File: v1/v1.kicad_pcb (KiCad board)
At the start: 2 copper layers, 48.3 x 30.5 mm, 11 parts, among them J3 PWR, J4 RGB, U1 Lolin/WeMos_D1_mini, U2 LevelShifter

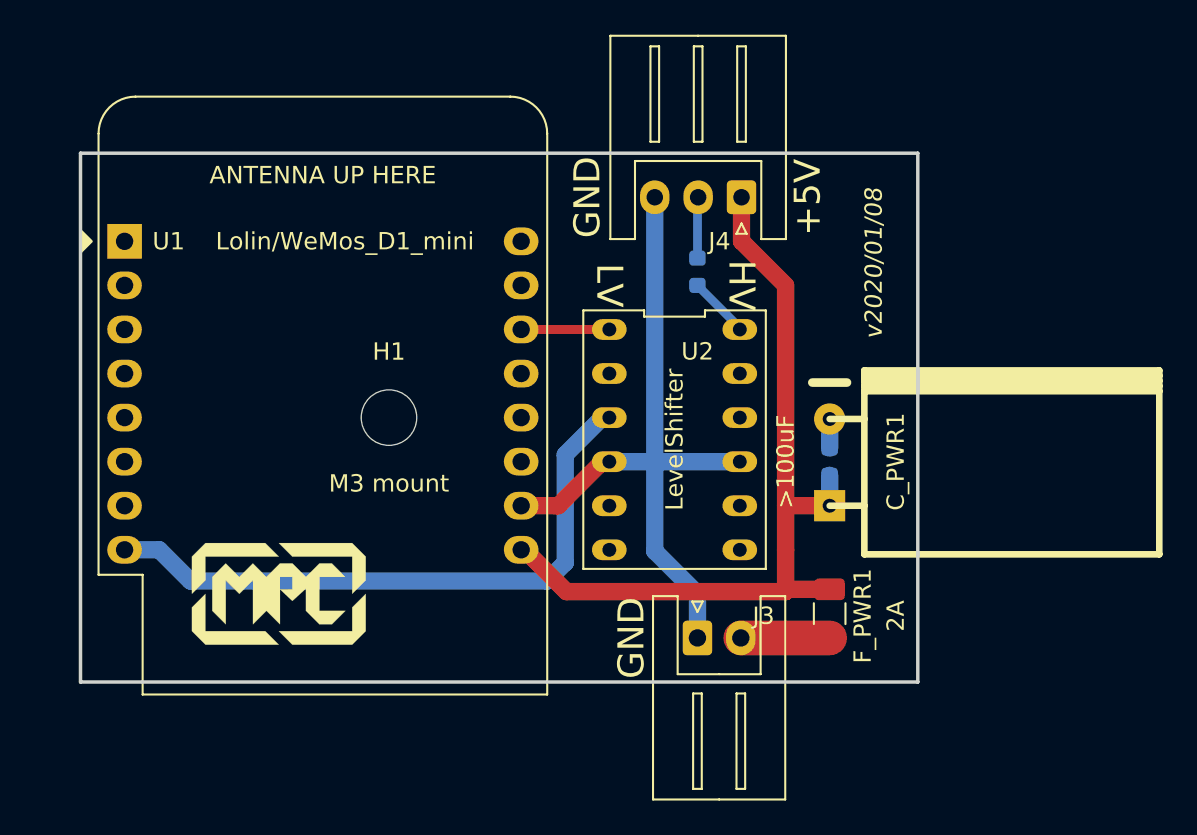
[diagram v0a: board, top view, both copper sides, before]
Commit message: fix level converter footprint
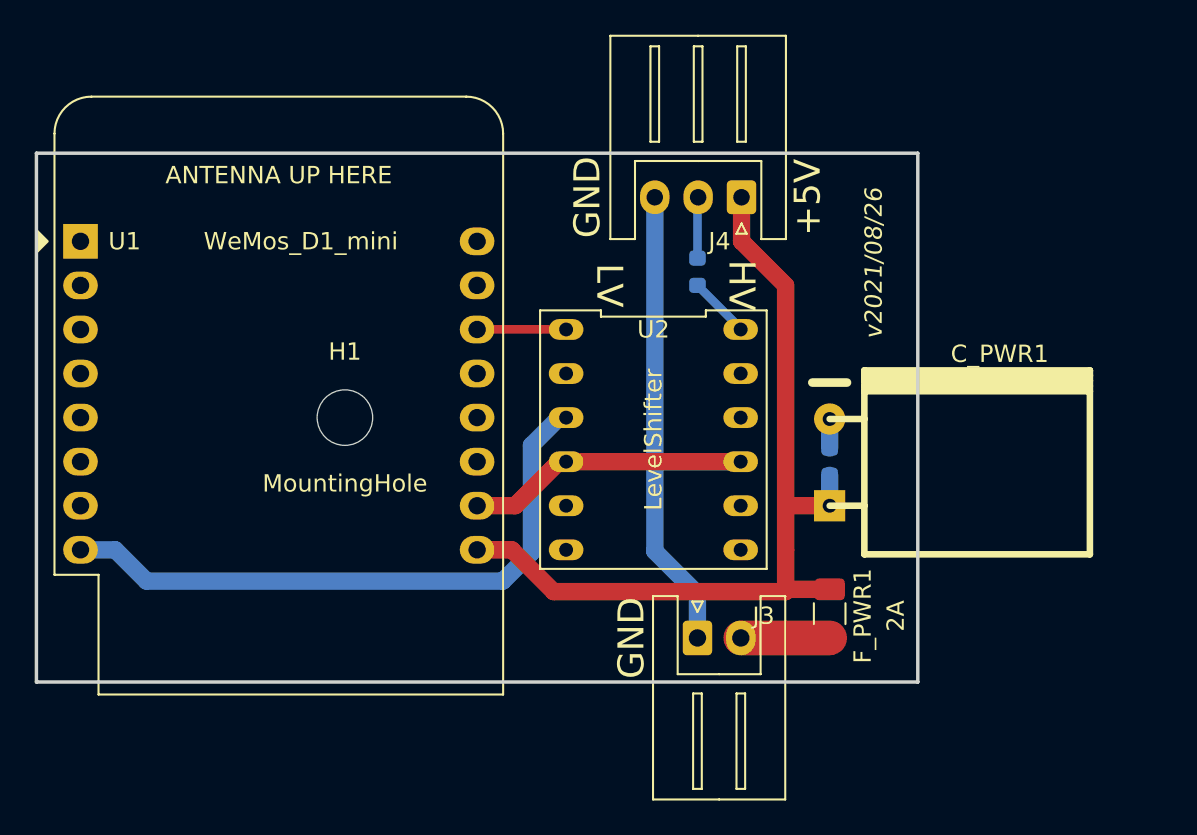
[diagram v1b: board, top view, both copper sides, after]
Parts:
- removed G***: LOGO, libs:mpc_logo_10mm
- removed G***: LOGO, MF custom:mpc_logo_10mm
- C_PWR1: footprint w_capacitors:CP_10x16mm_hor -> w_capacitors:CP_10x12.5mm_hor
- H1: value M3 mount -> MountingHole
- U1: value Lolin/WeMos_D1_mini -> WeMos_D1_mini
- moved H1 2.54 mm to (68.6, 66.0)
- moved U1 2.54 mm to (53.3, 55.9)
- moved C_PWR1 2.00 mm to (103.8, 68.6)
- moved U2 1.76 mm to (86.4, 66.0)
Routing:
- net GND: track 42.3 -> 49.3 mm
- net +5V: track 46.9 -> 49.5 mm
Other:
- board size 48.3 x 30.5 mm -> 50.8 x 30.5 mm
- board text added: "v2021/08/26"
- board text removed: "v2020/01/08"
